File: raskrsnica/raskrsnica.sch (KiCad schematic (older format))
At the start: 40 parts, among them J1 Screw_Terminal_01x02, U1 74HC595, U2 74HC595

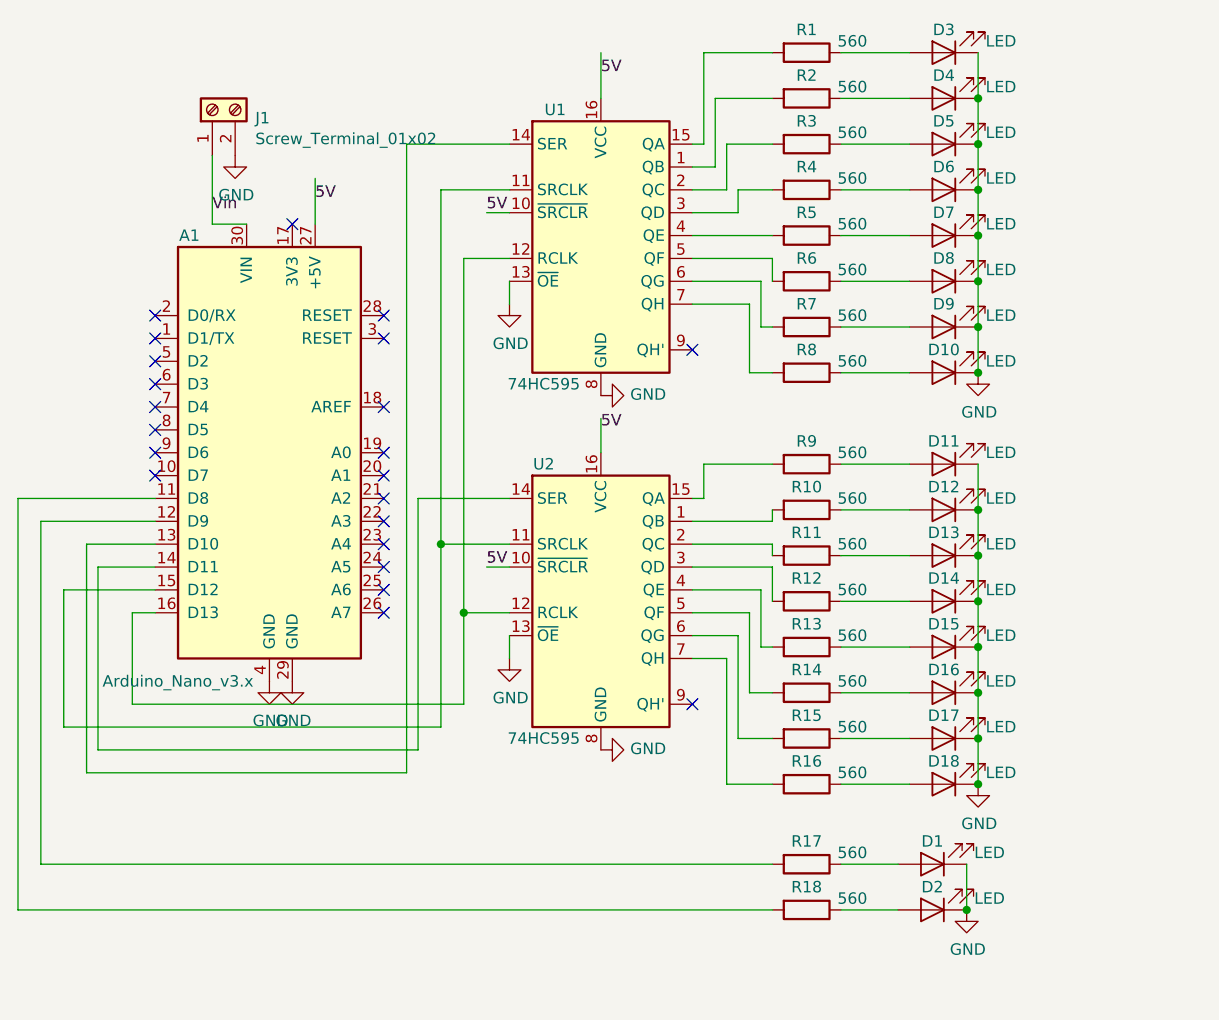
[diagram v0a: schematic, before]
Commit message: Raskrsnica sa konektorima -PCB not done
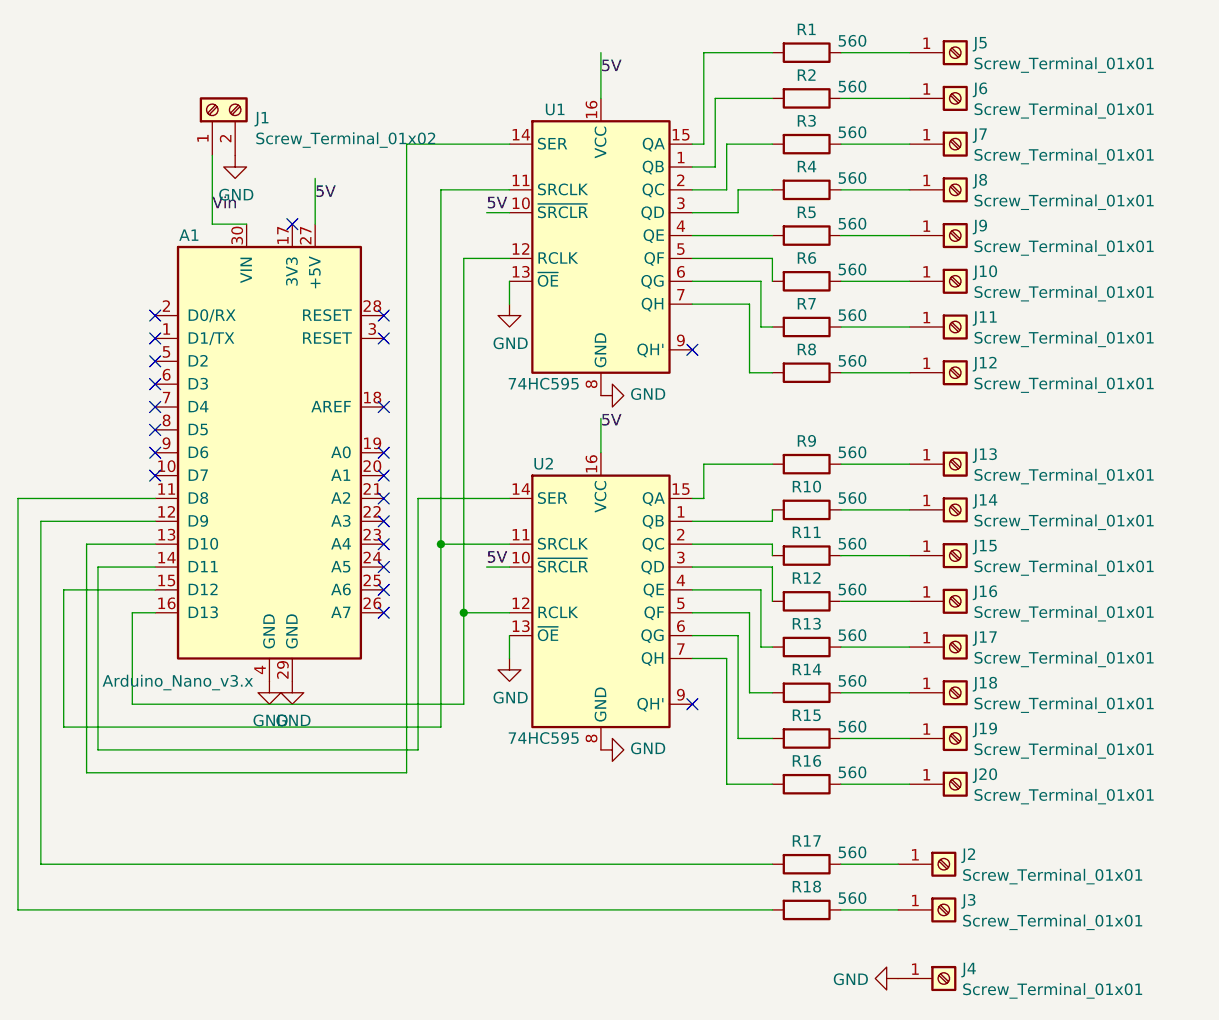
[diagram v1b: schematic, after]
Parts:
- removed D1, D10, D11, D12, D13, D14, D15, D16, D17, D2, D3, D4, D5, D6, D7, D8, D9: LED, LED_THT:LED_D5.0mm_Clear, symbol Device:LED
- removed D18: LED, Resistor_THT:R_Axial_DIN0207_L6.3mm_D2.5mm_P7.62mm_Horizontal, symbol Device:LED
- added J10, J11, J12, J13, J14, J15, J16, J17, J18, J19, J2, J20, J3, J4, J5, J6, J7, J8, J9: Screw_Terminal_01x01, TerminalBlock_MetzConnect:TerminalBlock_MetzConnect_360271_1x01_Horizontal_ScrewM3.0_Boxed, symbol Connector:Screw_Terminal_01x01
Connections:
- wire segments 114 -> 99

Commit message: Raskrsnica layout finished
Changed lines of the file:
@@
-	1    0    0    -1
-$EndComp
-$Comp
-L power:GND #PWR03
-U 1 1 5CC15199
-P 3300 3600
-F 0 "#PWR03" H 3300 3350 50  0001 C CNN
-F 1 "GND" H 3305 3427 50  0000 C CNN
-F 2 "" H 3300 3600 50  0001 C CNN
-F 3 "" H 3300 3600 50  0001 C CNN
-	1    3300 3600
 	1    0    0    -1
 $EndComp
